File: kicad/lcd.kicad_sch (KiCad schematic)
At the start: 1 part, among them J1 Conn_01x04_Socket

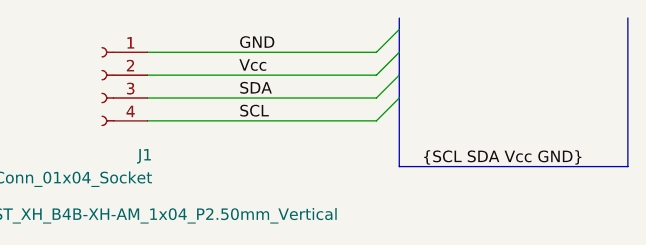
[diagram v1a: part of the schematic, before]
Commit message: aggiunto schema per motori PWM
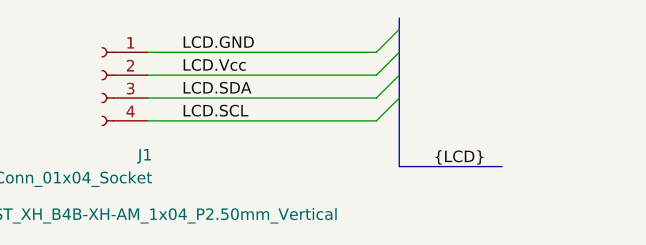
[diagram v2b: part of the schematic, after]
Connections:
- net GND renamed LCD.GND
- net SCL renamed LCD.SCL
- net SDA renamed LCD.SDA
- net Vcc renamed LCD.Vcc
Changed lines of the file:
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@@
 	)
 	(bus_entry
-		(at 80.01 39.37)
-		(size 2.54 -2.54)
+		(at 82.55 31.75)
+		(size -2.54 2.54)
 		(stroke
 			(width 0)
@@
 	)
 	(bus_entry
-		(at 80.01 31.75)
-		(size 2.54 -2.54)
+		(at 82.55 36.83)
+		(size -2.54 2.54)
 		(stroke
 			(width 0)
@@
 	)
 	(bus_entry
-		(at 80.01 36.83)
-		(size 2.54 -2.54)
+		(at 82.55 29.21)
+		(size -2.54 2.54)
 		(stroke
 			(width 0)
@@
 	)
 	(bus_entry
-		(at 80.01 34.29)
-		(size 2.54 -2.54)
+		(at 82.55 34.29)
+		(size -2.54 2.54)
+		(stroke
+			(width 0)
+			(type default)
+		)
+	)
+	(bus
+		(pts
+			(xy 82.55 29.21) (xy 82.55 31.75)
+		)
 		(stroke
 			(width 0)
@@
 		(pts
 			(xy 82.55 36.83) (xy 82.55 44.45)
+		)
+		(stroke
+			(width 0)
+			(type default)
+		)
+	)
+	(wire
+		(pts
+			(xy 54.61 39.37) (xy 80.01 39.37)
+		)
+		(stroke
+			(width 0)
+			(type default)
+		)
+	)
+	(wire
+		(pts
+			(xy 54.61 36.83) (xy 80.01 36.83)
 		)
 		(stroke
@@
 	(bus
 		(pts
-			(xy 82.55 44.45) (xy 107.95 44.45)
-		)
-		(stroke
-			(width 0)
-			(type default)
-		)
-	)
-	(bus
-		(pts
-			(xy 82.55 29.21) (xy 82.55 31.75)
+			(xy 82.55 44.45) (xy 93.98 44.45)
 		)
 		(stroke
@@
 	(wire
 		(pts
-			(xy 54.61 36.83) (xy 80.01 36.83)
+			(xy 54.61 31.75) (xy 80.01 31.75)
 		)
 		(stroke
@@
 		)
 	)
+	(bus
+		(pts
+			(xy 82.55 31.75) (xy 82.55 34.29)
+		)
+		(stroke
+			(width 0)
+			(type default)
+		)
+	)
 	(wire
 		(pts
@@
 		)
 	)
-	(wire
-		(pts
-			(xy 54.61 31.75) (xy 80.01 31.75)
-		)
-		(stroke
-			(width 0)
-			(type default)
-		)
-	)
-	(wire
-		(pts
-			(xy 54.61 39.37) (xy 80.01 39.37)
-		)
-		(stroke
-			(width 0)
-			(type default)
-		)
-	)
-	(bus
-		(pts
-			(xy 82.55 31.75) (xy 82.55 34.29)
-		)
-		(stroke
-			(width 0)
-			(type default)
-		)
-	)
-	(bus
-		(pts
-			(xy 107.95 27.94) (xy 107.95 44.45)
-		)
-		(stroke
-			(width 0)
-			(type default)
-		)
-	)
-	(label "SCL"
-		(at 64.77 39.37 0)
+	(label "LCD.Vcc"
+		(at 58.42 34.29 0)
 		(effects
 			(font
@@
 		)
 	)
-	(label "SDA"
-		(at 64.77 36.83 0)
+	(label "LCD.GND"
+		(at 58.42 31.75 0)
 		(effects
 			(font
@@
 		)
 	)
-	(label "GND"
-		(at 64.77 31.75 0)
+	(label "LCD.SCL"
+		(at 58.42 39.37 0)
 		(effects
 			(font
@@
 		)
 	)
-	(label "{SCL SDA Vcc GND}"
-		(at 85.09 44.45 0)
+	(label "{LCD}"
+		(at 86.36 44.45 0)
 		(effects
 			(font
@@
 		)
 	)
-	(label "Vcc"
-		(at 64.77 34.29 0)
+	(label "LCD.SDA"
+		(at 58.42 36.83 0)
 		(effects
 			(font

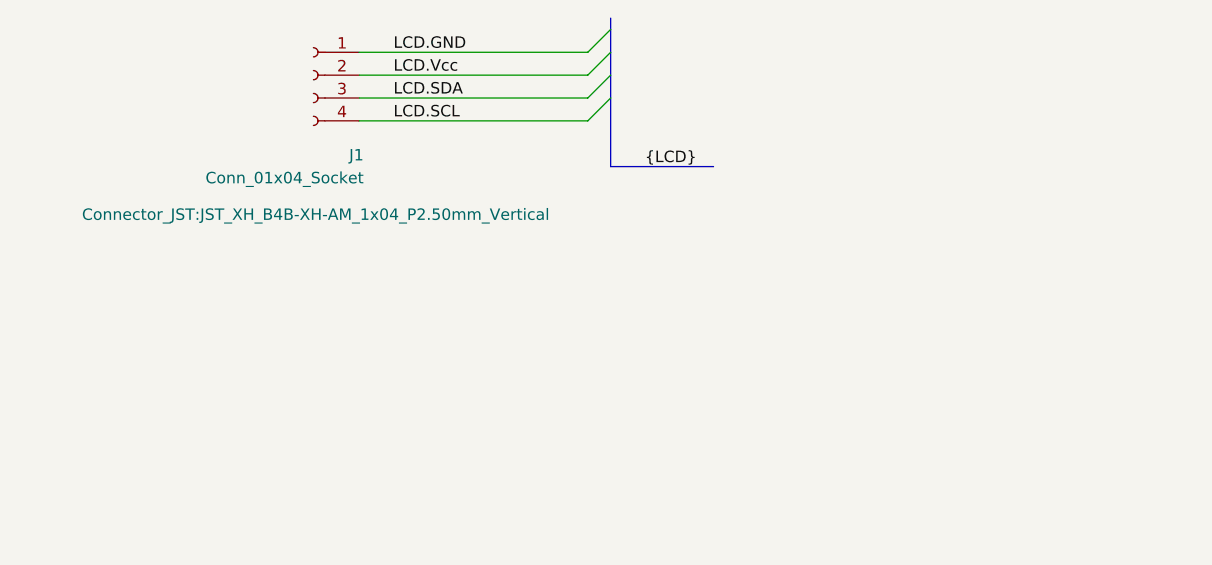
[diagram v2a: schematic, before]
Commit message: adding pull-up resistor to I2C interface connection
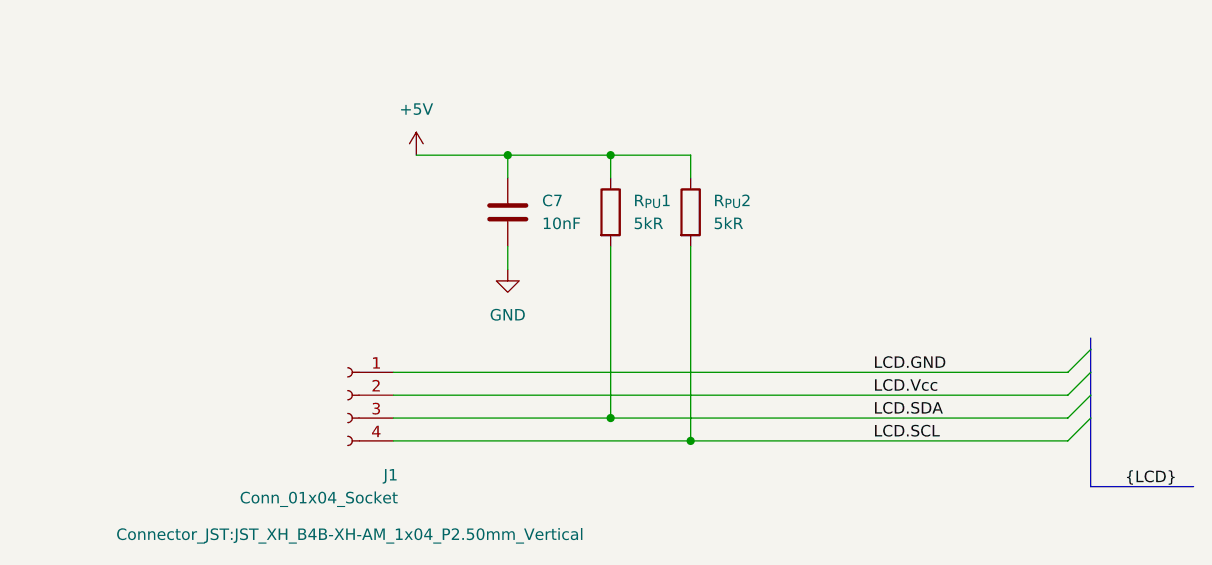
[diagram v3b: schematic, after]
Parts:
- added C7: 10nF, Capacitor_THT:C_Disc_D5.0mm_W2.5mm_P5.00mm, symbol Device:C
- added R_{PU}1, R_{PU}2: 5kR, symbol Device:R
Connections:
- net LCD.SCL: now also R_{PU}2.2
- net LCD.SDA: now also R_{PU}1.2
- new net +5V: C7.1, R_{PU}1.1, R_{PU}2.1
- new net GND: C7.2
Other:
- moved on the sheet: J1
